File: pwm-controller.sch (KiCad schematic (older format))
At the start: 36 parts, among them J1 DEBUG_ADDRESS_I2C_INT, J2 POWER, J3 OUT+, J4 OUT-, SW1 EC12D1524403, U1 STM8S003F3Px, U2 78L05

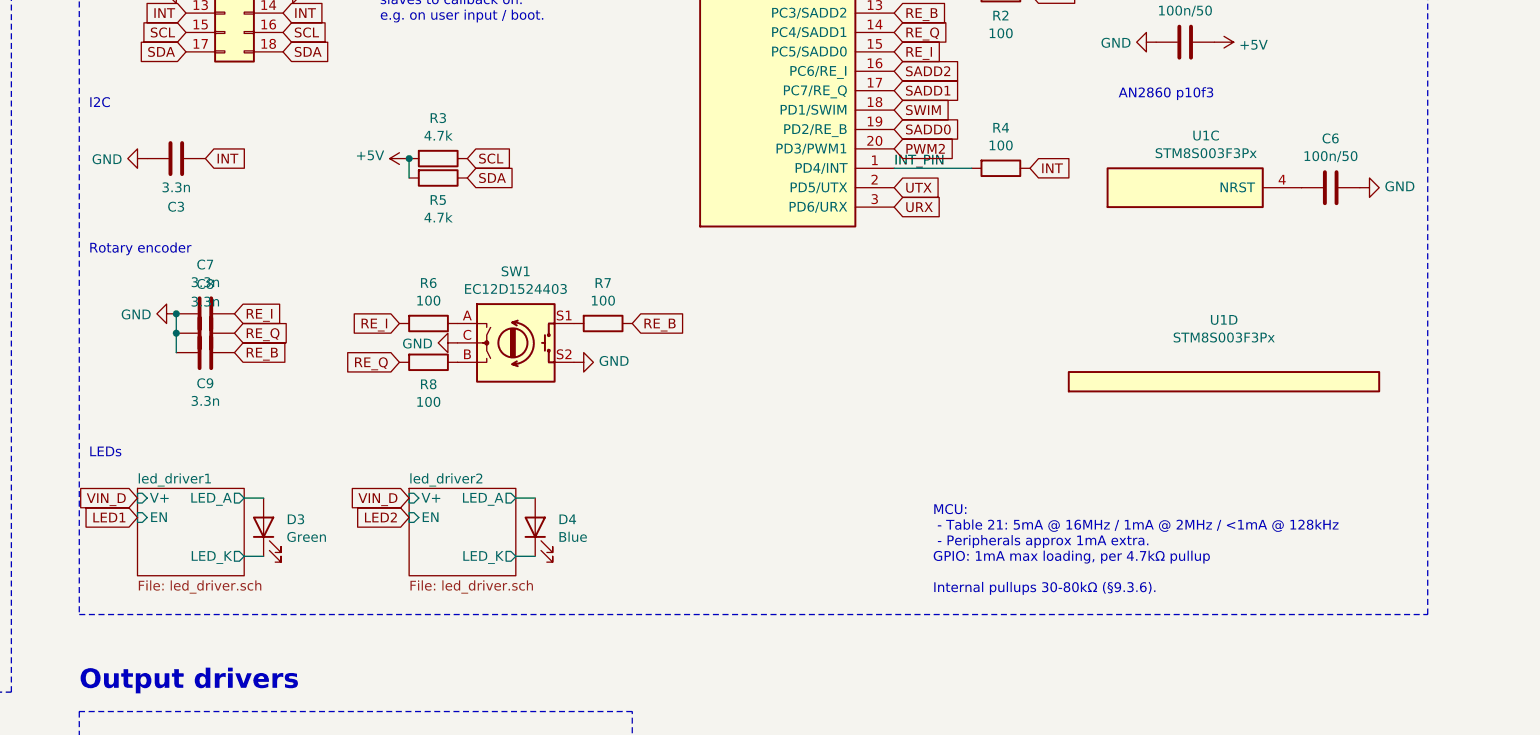
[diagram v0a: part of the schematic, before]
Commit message: swapped placement for 5V LDO vs LEDs, for more stable 5V supply when power-side of ground is noisy
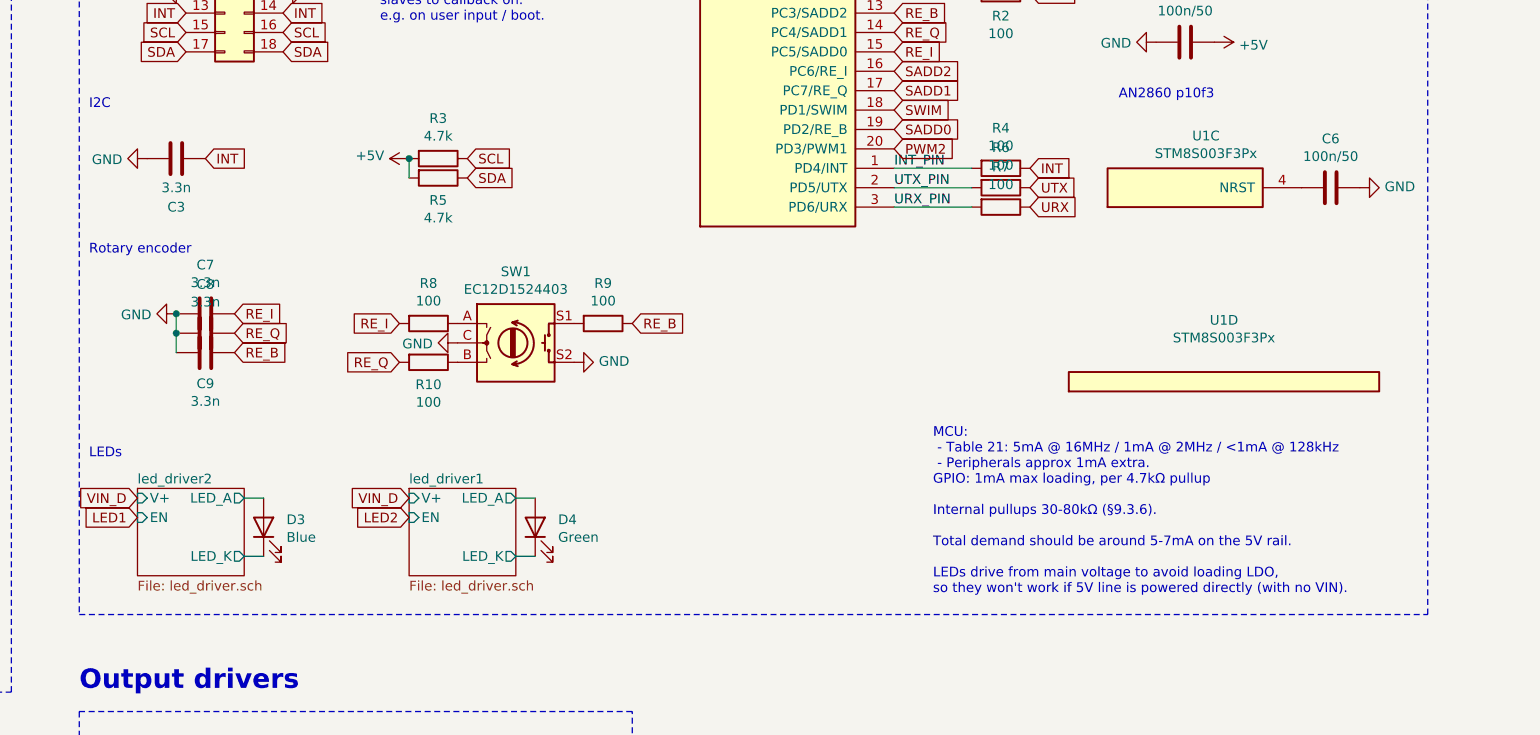
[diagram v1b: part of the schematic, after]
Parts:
- added R6, R7: 100, Resistor_SMD:R_0402_1005Metric, symbol Device:R
- renumbered D4 to D3, D3 to D4, R8 to R10, R6 to R8, R7 to R9
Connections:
- net URX: now also R7.1; no longer U1.3 (PD6/URX)
- net UTX: now also R6.1; no longer U1.2 (PD5/UTX)
- new net URX_PIN: R7.2, U1.3 (PD6/URX)
- new net UTX_PIN: R6.2, U1.2 (PD5/UTX)
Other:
- note added: "MCU:\n - Table 21: 5mA @ 16MHz / 1mA @ 2MHz / <1mA @ 128kHz\n - Peripherals approx 1mA extra.\nGPIO: 1mA max loading, per 4.7kΩ pullup\n\nInternal pullups 30-80kΩ (§9.3.6).\n\nTotal demand should be around 5-7mA on the 5V rail.\n\nLEDs drive from main voltage to avoid loading LDO,\nso they won't work if 5V line is powered directly (with no VIN)."
- note removed: "MCU:\n - Table 21: 5mA @ 16MHz / 1mA @ 2MHz / <1mA @ 128kHz\n - Peripherals approx 1mA extra.\nGPIO: 1mA max loading, per 4.7kΩ pullup\n\nInternal pullups 30-80kΩ (§9.3.6)."
- moved on the sheet: D3, D4
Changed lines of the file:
@@
 Text GLabel 8150 2500 2    50   Input ~ 0
 PWM1
-Text GLabel 8150 3700 2    50   Input ~ 0
+Text GLabel 8850 3700 2    50   Input ~ 0
 UTX
-Text GLabel 8150 3800 2    50   Input ~ 0
+Text GLabel 8850 3800 2    50   Input ~ 0
 URX
 Text GLabel 5950 3550 2    50   Input ~ 0
@@
 <10mA for control+driver, <10A for target
 $Comp
-L Device:LED D3
+L Device:LED D4
 U 1 1 61F68833
-P 4900 5450
-F 0 "D3" V 4939 5332 50  0000 R CNN
-F 1 "Green" V 4848 5332 50  0000 R CNN
-F 2 "LED_SMD:LED_0603_1608Metric" H 4900 5450 50  0001 C CNN
-F 3 "https://datasheet.lcsc.com/lcsc/1811101510_Everlight-Elec-19-217-GHC-YR1S2-3T_C72043.pdf" H 4900 5450 50  0001 C CNN
-F 4 "C72043" H 4900 5450 50  0001 C CNN "JLC"
-	1    4900 5450
+P 6300 5450
+F 0 "D4" V 6339 5332 50  0000 R CNN
+F 1 "Green" V 6248 5332 50  0000 R CNN
+F 2 "LED_SMD:LED_0603_1608Metric" H 6300 5450 50  0001 C CNN
+F 3 "https://datasheet.lcsc.com/lcsc/1811101510_Everlight-Elec-19-217-GHC-YR1S2-3T_C72043.pdf" H 6300 5450 50  0001 C CNN
+F 4 "C72043" H 6300 5450 50  0001 C CNN "JLC"
+	1    6300 5450
 	0    -1   -1   0
 $EndComp
@@
 Rotary encoder
 $Comp
-L Device:LED D4
+L Device:LED D3
 U 1 1 61F7EFE5
-P 6300 5450
-F 0 "D4" V 6339 5332 50  0000 R CNN
-F 1 "Blue" V 6248 5332 50  0000 R CNN
-F 2 "LED_SMD:LED_0603_1608Metric" H 6300 5450 50  0001 C CNN
-F 3 "https://datasheet.lcsc.com/lcsc/1811101510_Everlight-Elec-19-217-BHC-ZL1M2RY-3T_C72041.pdf" H 6300 5450 50  0001 C CNN
-F 4 "C72041" H 6300 5450 50  0001 C CNN "JLC"
-	1    6300 5450
+P 4900 5450
+F 0 "D3" V 4939 5332 50  0000 R CNN
+F 1 "Blue" V 4848 5332 50  0000 R CNN
+F 2 "LED_SMD:LED_0603_1608Metric" H 4900 5450 50  0001 C CNN
+F 3 "https://datasheet.lcsc.com/lcsc/1811101510_Everlight-Elec-19-217-BHC-ZL1M2RY-3T_C72041.pdf" H 4900 5450 50  0001 C CNN
+F 4 "C72041" H 4900 5450 50  0001 C CNN "JLC"
+	1    4900 5450
 	0    -1   -1   0
 $EndComp
@@
 AR Path="/61C031A1/61CD939B" Ref="R?"  Part="1"
 AR Path="/61C031A3/61CD939B" Ref="R?"  Part="1"
-AR Path="/61CD939B" Ref="R6"  Part="1"
-F 0 "R6" V 5543 4400 50  0000 C CNN
+AR Path="/61CD939B" Ref="R8"  Part="1"
+F 0 "R8" V 5543 4400 50  0000 C CNN
 F 1 "100" V 5634 4400 50  0000 C CNN
 F 2 "Resistor_SMD:R_0402_1005Metric" V 5680 4400 50  0001 C CNN
@@
 AR Path="/61C031A1/61CD98C2" Ref="R?"  Part="1"
 AR Path="/61C031A3/61CD98C2" Ref="R?"  Part="1"
-AR Path="/61CD98C2" Ref="R8"  Part="1"
-F 0 "R8" V 5865 4600 50  0000 C CNN
+AR Path="/61CD98C2" Ref="R10"  Part="1"
+F 0 "R10" V 5865 4600 50  0000 C CNN
 F 1 "100" V 5956 4600 50  0000 C CNN
 F 2 "Resistor_SMD:R_0402_1005Metric" V 5680 4600 50  0001 C CNN
@@
 AR Path="/61C031A1/61CDA382" Ref="R?"  Part="1"
 AR Path="/61C031A3/61CDA382" Ref="R?"  Part="1"
-AR Path="/61CDA382" Ref="R7"  Part="1"
-F 0 "R7" V 6443 4400 50  0000 C CNN
+AR Path="/61CDA382" Ref="R9"  Part="1"
+F 0 "R9" V 6443 4400 50  0000 C CNN
 F 1 "100" V 6534 4400 50  0000 C CNN
 F 2 "Resistor_SMD:R_0402_1005Metric" V 6580 4400 50  0001 C CNN
@@
 PWM1
 Text Notes 8350 5800 0    50   ~ 0
-MCU:\n - Table 21: 5mA @ 16MHz / 1mA @ 2MHz / <1mA @ 128kHz\n - Peripherals approx 1mA extra.\nGPIO: 1mA max loading, per 4.7kΩ pullup\n\nInternal pullups 30-80kΩ (§9.3.6).
+MCU:\n - Table 21: 5mA @ 16MHz / 1mA @ 2MHz / <1mA @ 128kHz\n - Peripherals approx 1mA extra.\nGPIO: 1mA max loading, per 4.7kΩ pullup\n\nInternal pullups 30-80kΩ (§9.3.6).\n\nTotal demand should be around 5-7mA on the 5V rail.\n\nLEDs drive from main voltage to avoid loading LDO,\nso they won't work if 5V line is powered directly (with no VIN).
 Wire Notes Line
 	6800 6400 3950 6400
@@
 	2900 3450 3200 3450
 $Sheet
-S 4250 5250 550  450
+S 5650 5250 550  450
 U 61D242FF
 F0 "led_driver1" 50
 F1 "led_driver.sch" 50
-F2 "EN" I L 4250 5400 50
-F3 "V+" I L 4250 5300 50
-F4 "LED_A" O R 4800 5300 50
-F5 "LED_K" O R 4800 5600 50
+F2 "EN" I L 5650 5400 50
+F3 "V+" I L 5650 5300 50
+F4 "LED_A" O R 6200 5300 50
+F5 "LED_K" O R 6200 5600 50
 $EndSheet
 Wire Wire Line
-	4800 5300 4900 5300
-Wire Wire Line
-	4900 5600 4800 5600
+	6200 5300 6300 5300
+Wire Wire Line
+	6300 5600 6200 5600
 Text GLabel 4250 5300 0    50   Input ~ 0
 VIN_D
@@
 LEDs
 $Sheet
-S 5650 5250 550  450
+S 4250 5250 550  450
 U 61D33B82
 F0 "led_driver2" 50
 F1 "led_driver.sch" 50
-F2 "EN" I L 5650 5400 50
-F3 "V+" I L 5650 5300 50
-F4 "LED_A" O R 6200 5300 50
-F5 "LED_K" O R 6200 5600 50
+F2 "EN" I L 4250 5400 50
+F3 "V+" I L 4250 5300 50
+F4 "LED_A" O R 4800 5300 50
+F5 "LED_K" O R 4800 5600 50
 $EndSheet
 Wire Wire Line
-	6200 5300 6300 5300
-Wire Wire Line
-	6300 5600 6200 5600
+	4800 5300 4900 5300
+Wire Wire Line
+	4900 5600 4800 5600
 Text GLabel 5650 5300 0    50   Input ~ 0
 VIN_D
@@
 Text Label 8150 3600 0    50   ~ 0
 INT_PIN
+$Comp
+L Device:R R?
+U 1 1 623F661A
+P 8700 3700
+AR Path="/61B5C5B6/623F661A" Ref="R?"  Part="1"
+AR Path="/61C03040/623F661A" Ref="R?"  Part="1"
+AR Path="/61C031A1/623F661A" Ref="R?"  Part="1"
+AR Path="/61C031A3/623F661A" Ref="R?"  Part="1"
+AR Path="/623F661A" Ref="R6"  Part="1"
+F 0 "R6" V 8493 3700 50  0000 C CNN
+F 1 "100" V 8584 3700 50  0000 C CNN
+F 2 "Resistor_SMD:R_0402_1005Metric" V 8630 3700 50  0001 C CNN
+F 3 "~" H 8700 3700 50  0001 C CNN
+F 4 "C25076" H 8700 3700 50  0001 C CNN "JLC"
+	1    8700 3700
+	0    1    1    0
+$EndComp
+$Comp
+L Device:R R?
+U 1 1 623F6E05
+P 8700 3800
+AR Path="/61B5C5B6/623F6E05" Ref="R?"  Part="1"
+AR Path="/61C03040/623F6E05" Ref="R?"  Part="1"
+AR Path="/61C031A1/623F6E05" Ref="R?"  Part="1"
+AR Path="/61C031A3/623F6E05" Ref="R?"  Part="1"
+AR Path="/623F6E05" Ref="R7"  Part="1"
+F 0 "R7" V 8493 3800 50  0000 C CNN
+F 1 "100" V 8584 3800 50  0000 C CNN
+F 2 "Resistor_SMD:R_0402_1005Metric" V 8630 3800 50  0001 C CNN
+F 3 "~" H 8700 3800 50  0001 C CNN
+F 4 "C25076" H 8700 3800 50  0001 C CNN "JLC"
+	1    8700 3800
+	0    1    1    0
+$EndComp
+Wire Wire Line
+	8150 3700 8550 3700
+Wire Wire Line
+	8550 3800 8150 3800
+Text Label 8150 3700 0    50   ~ 0
+UTX_PIN
+Text Label 8150 3800 0    50   ~ 0
+URX_PIN
 $EndSCHEMATC

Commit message: order ready
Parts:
- added G1: Roger, pwm-controller:roger, symbol Mechanical:MountingHole
- C2, C5, C6: value 100n/50 -> 100n; JLC C307331 -> C1525
- C3, C7, C8, C9: value 3.3n -> 100n; JLC C26404 -> C1525
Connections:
- net INT: no longer C3.2
- net INT_PIN: now also C3.2
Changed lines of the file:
@@
 AR Path="/61B5C5B6/61BEA8AF" Ref="C?"  Part="1"
 F 0 "C5" H 3015 3646 50  0000 L CNN
-F 1 "100n/50" H 3015 3555 50  0000 L CNN
+F 1 "100n" H 3015 3555 50  0000 L CNN
 F 2 "Capacitor_SMD:C_0402_1005Metric" H 2938 3450 50  0001 C CNN
 F 3 "~" H 2900 3600 50  0001 C CNN
-F 4 "C307331" H 2900 3600 50  0001 C CNN "JLC"
+F 4 "C1525" H 2900 3600 50  0001 C CNN "JLC"
 	1    2900 3600
 	1    0    0    -1
@@
 AR Path="/61C031A3/61BBD7AA" Ref="C?"  Part="1"
 F 0 "C6" V 10652 3700 50  0000 C CNN
-F 1 "100n/50" V 10561 3700 50  0000 C CNN
+F 1 "100n" V 10561 3700 50  0000 C CNN
 F 2 "Capacitor_SMD:C_0402_1005Metric" H 10438 3550 50  0001 C CNN
 F 3 "~" H 10400 3700 50  0001 C CNN
-F 4 "C307331" H 10400 3700 50  0001 C CNN "JLC"
+F 4 "C1525" H 10400 3700 50  0001 C CNN "JLC"
 	1    10400 3700
 	0    -1   -1   0
@@
 AR Path="/61C031A3/61BC782F" Ref="C?"  Part="1"
 F 0 "C2" V 9902 2950 50  0000 C CNN
-F 1 "100n/50" V 9811 2950 50  0000 C CNN
+F 1 "100n" V 9811 2950 50  0000 C CNN
 F 2 "Capacitor_SMD:C_0402_1005Metric" H 9688 2800 50  0001 C CNN
 F 3 "~" H 9650 2950 50  0001 C CNN
-F 4 "C307331" H 9650 2950 50  0001 C CNN "JLC"
+F 4 "C1525" H 9650 2950 50  0001 C CNN "JLC"
 	1    9650 2950
 	0    -1   -1   0
@@
 AR Path="/61C031A3/62237167" Ref="C?"  Part="1"
 F 0 "C7" V 4852 4350 50  0000 C CNN
-F 1 "3.3n" V 4761 4350 50  0000 C CNN
+F 1 "100n" V 4761 4350 50  0000 C CNN
 F 2 "Capacitor_SMD:C_0402_1005Metric" H 4638 4200 50  0001 C CNN
 F 3 "~" H 4600 4350 50  0001 C CNN
-F 4 "C26404" H 4600 4350 50  0001 C CNN "JLC"
+F 4 "C1525" H 4600 4350 50  0001 C CNN "JLC"
 	1    4600 4350
 	0    -1   -1   0
@@
 AR Path="/61C031A3/62237A30" Ref="C?"  Part="1"
 F 0 "C8" V 4852 4450 50  0000 C CNN
-F 1 "3.3n" V 4761 4450 50  0000 C CNN
+F 1 "100n" V 4761 4450 50  0000 C CNN
 F 2 "Capacitor_SMD:C_0402_1005Metric" H 4638 4300 50  0001 C CNN
 F 3 "~" H 4600 4450 50  0001 C CNN
-F 4 "C26404" H 4600 4450 50  0001 C CNN "JLC"
+F 4 "C1525" H 4600 4450 50  0001 C CNN "JLC"
 	1    4600 4450
 	0    -1   -1   0
@@
 AR Path="/61C031A3/62237C27" Ref="C?"  Part="1"
 F 0 "C9" V 4440 4550 50  0000 C CNN
-F 1 "3.3n" V 4349 4550 50  0000 C CNN
+F 1 "100n" V 4349 4550 50  0000 C CNN
 F 2 "Capacitor_SMD:C_0402_1005Metric" H 4638 4400 50  0001 C CNN
 F 3 "~" H 4600 4550 50  0001 C CNN
-F 4 "C26404" H 4600 4550 50  0001 C CNN "JLC"
+F 4 "C1525" H 4600 4550 50  0001 C CNN "JLC"
 	1    4600 4550
 	0    -1   -1   0
@@
 	1    0    0    -1
 $EndComp
-Text GLabel 4600 3550 2    50   Input ~ 0
-INT
 $Comp
 L Device:C C3
@@
 AR Path="/61C031A3/61F9A9FB" Ref="C?"  Part="1"
 F 0 "C3" V 4200 3550 50  0000 C CNN
-F 1 "3.3n" V 4300 3550 50  0000 C CNN
+F 1 "100n" V 4300 3550 50  0000 C CNN
 F 2 "Capacitor_SMD:C_0402_1005Metric" H 4488 3400 50  0001 C CNN
 F 3 "~" H 4450 3550 50  0001 C CNN
-F 4 "C26404" H 4450 3550 50  0001 C CNN "JLC"
+F 4 "C1525" H 4450 3550 50  0001 C CNN "JLC"
 	1    4450 3550
 	0    -1   -1   0
@@
 Text Label 8150 3800 0    50   ~ 0
 URX_PIN
+$Comp
+L Mechanical:MountingHole G1
+U 1 1 6246AF29
+P 3100 7050
+F 0 "G1" H 3200 7096 50  0000 L CNN
+F 1 "Roger" H 3200 7005 50  0000 L CNN
+F 2 "pwm-controller:roger" H 3100 7050 50  0001 C CNN
+F 3 "~" H 3100 7050 50  0001 C CNN
+F 4 "-" H 3100 7050 50  0001 C CNN "JLC"
+	1    3100 7050
+	1    0    0    -1
+$EndComp
+Text Label 4600 3550 0    50   ~ 0
+INT_PIN
 $EndSCHEMATC

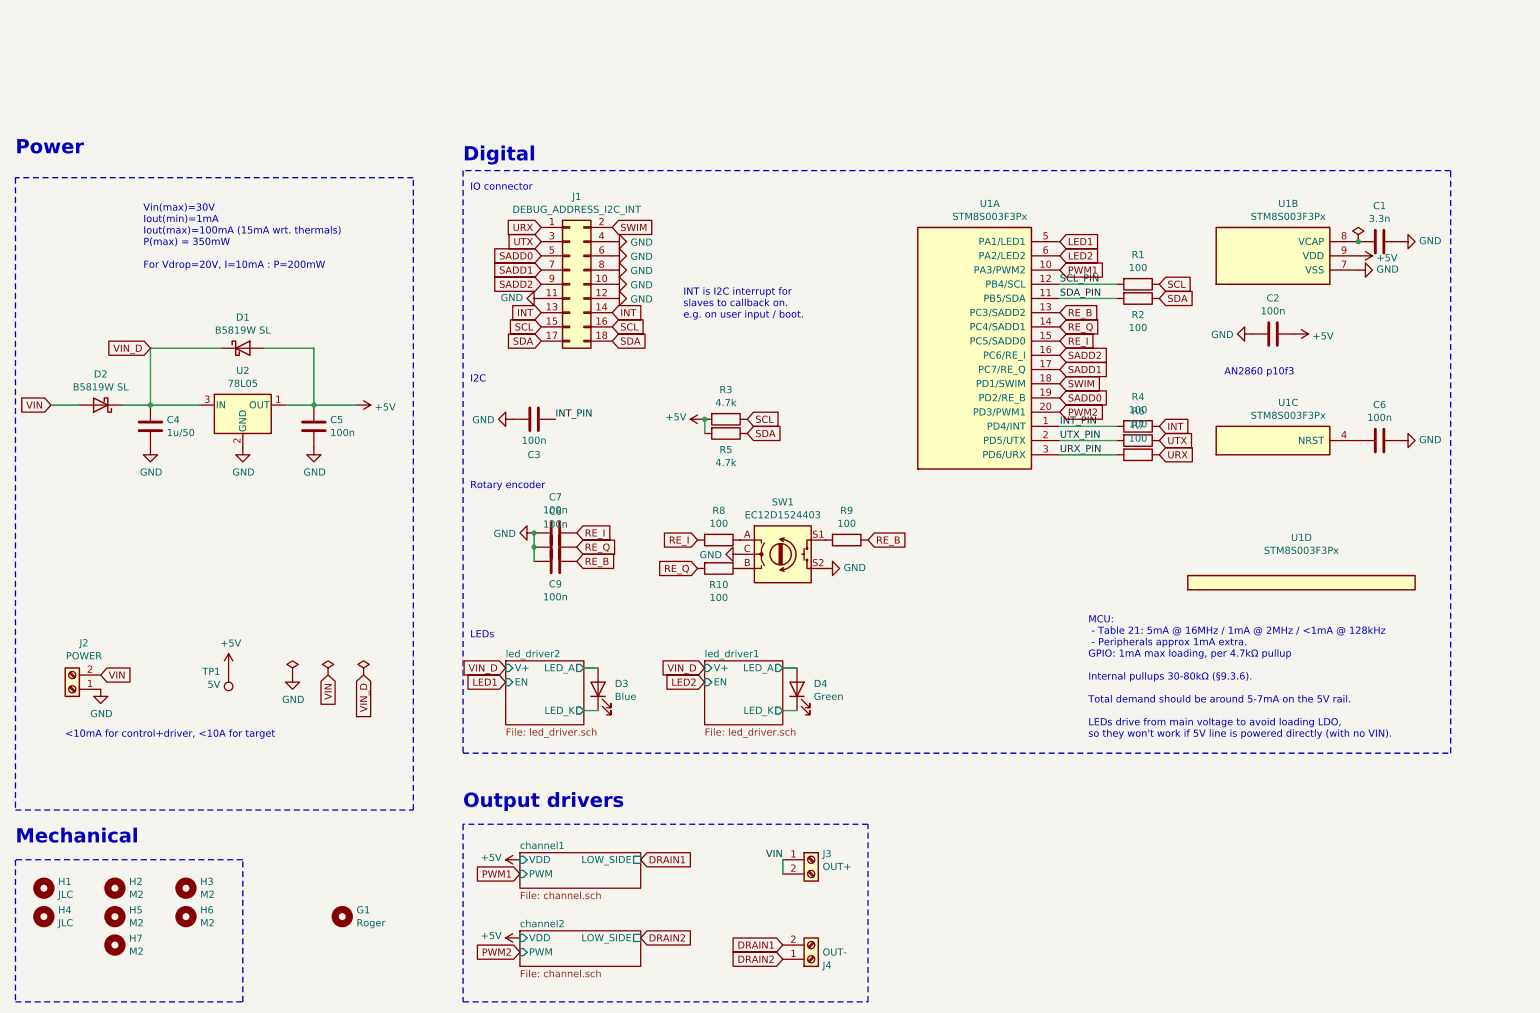
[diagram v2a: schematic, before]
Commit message: exposed NRST
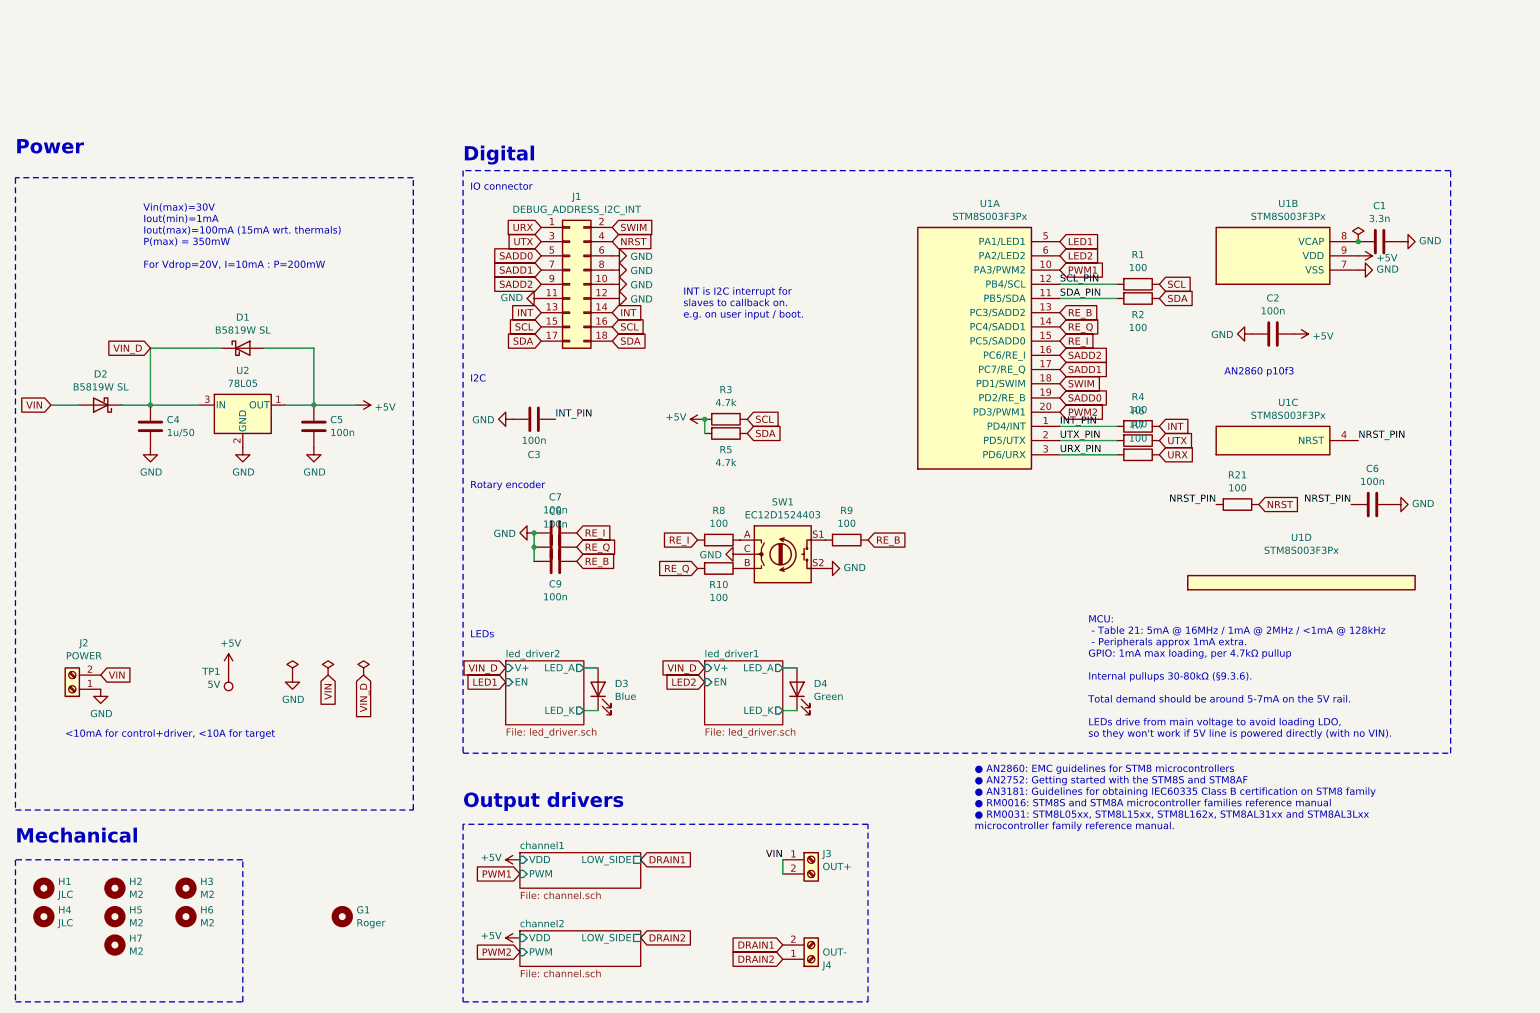
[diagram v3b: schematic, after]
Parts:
- added R21: 100, Resistor_SMD:R_0402_1005Metric, symbol Device:R
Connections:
- net GND: no longer J1.4 (Pin_4)
- net NRST_PIN: now reaches C6.1, U1.4 (NRST)
- net NRST_PIN: now also R21.2
- new net NRST: J1.4 (Pin_4), R21.1
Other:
- note added: "● AN2860: EMC guidelines for STM8 microcontrollers\n● AN2752: Getting started with the STM8S and STM8AF\n● AN3181: Guidelines for obtaining IEC60335 Class B certification on STM8 family\n● RM0016: STM8S and STM8A microcontroller families reference manual\n● RM0031: STM8L05xx, STM8L15xx, STM8L162x, STM8AL31xx and STM8AL3Lxx\nmicrocontroller family reference manual."
- moved on the sheet: C6
